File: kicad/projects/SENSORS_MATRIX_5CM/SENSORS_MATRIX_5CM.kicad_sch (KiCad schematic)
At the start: 15 parts, among them J1 Conn_02x11_Odd_Even

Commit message: sensors board almost finished
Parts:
- C1: LCSC p/n (none) -> C24123
- C2: MP CL21A105KOFNNNE -> (none); shop https://www.lcsc.com/product-detail/Multilayer-Ceramic-Capa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 -> (none)
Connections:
- net +3V3: now also J1.11 (Pin_11), J1.12 (Pin_12); no longer J1.2 (Pin_2), J1.20 (Pin_20)
- net FBK_3V3_SENSORS: now also J1.14 (Pin_14); no longer J1.19 (Pin_19)
- net GND: now also J1.20 (Pin_20)
- net SIG1: now also J1.2 (Pin_2); no longer J1.11 (Pin_11)
- net SIG2: now also J1.15 (Pin_15); no longer J1.14 (Pin_14)
- net SIG3: now also J1.18 (Pin_18); no longer J1.15 (Pin_15)
- net SIG4: now also J1.19 (Pin_19); no longer J1.18 (Pin_18)
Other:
- moved on the sheet: C1, C2, D1, D2, D3, D4, D5, J1, R26, R27, R3, R4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

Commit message: brain v2, all components placed?
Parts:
- J1: footprint Connector_PinSocket_2.54mm:PinSocket_2x11_P2.54mm_Horizontal -> Connector_PinHeader_2.54mm:PinHeader_2x11_P2.54mm_Horizontal
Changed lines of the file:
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@@
 	)
 	(junction
+		(at 161.29 63.5)
+		(diameter 0)
+		(color 0 0 0 0)
+	)
+	(junction
 		(at 217.17 54.61)
 		(diameter 0)
@@
 	)
 	(junction
+		(at 124.46 67.31)
+		(diameter 0)
+		(color 0 0 0 0)
+	)
+	(junction
 		(at 222.25 54.61)
 		(diameter 0)
@@
 	(wire
 		(pts
+			(xy 124.46 67.31) (xy 144.78 67.31)
+		)
+		(stroke
+			(width 0)
+			(type default)
+		)
+	)
+	(wire
+		(pts
 			(xy 157.48 69.85) (xy 165.1 69.85)
 		)
@@
 	(wire
 		(pts
-			(xy 121.92 67.31) (xy 144.78 67.31)
+			(xy 121.92 67.31) (xy 124.46 67.31)
 		)
 		(stroke
@@
 	(wire
 		(pts
+			(xy 161.29 63.5) (xy 132.08 63.5)
+		)
+		(stroke
+			(width 0)
+			(type default)
+		)
+	)
+	(wire
+		(pts
 			(xy 157.48 92.71) (xy 165.1 92.71)
 		)
@@
 	(wire
 		(pts
-			(xy 167.64 63.5) (xy 132.08 63.5)
+			(xy 167.64 63.5) (xy 161.29 63.5)
 		)
 		(stroke
@@
 	)
 	(symbol
+		(lib_id "power:PWR_FLAG")
+		(at 161.29 63.5 0)
+		(unit 1)
+		(exclude_from_sim no)
+		(in_bom yes)
+		(on_board yes)
+		(dnp no)
+		(fields_autoplaced yes)
+		(property "Reference" "#FLG01"
+			(at 161.29 61.595 0)
+			(effects
+				(font
+					(size 1.27 1.27)
+				)
+				(hide yes)
+			)
+		)
+		(property "Value" "PWR_FLAG"
+			(at 161.29 58.42 0)
+			(effects
+				(font
+					(size 1.27 1.27)
+				)
+			)
+		)
+		(property "Footprint" ""
+			(at 161.29 63.5 0)
+			(effects
+				(font
+					(size 1.27 1.27)
+				)
+				(hide yes)
+			)
+		)
+		(property "Datasheet" "~"
+			(at 161.29 63.5 0)
+			(effects
+				(font
+					(size 1.27 1.27)
+				)
+				(hide yes)
+			)
+		)
+		(property "Description" "Special symbol for telling ERC where power comes from"
+			(at 161.29 63.5 0)
+			(effects
+				(font
+					(size 1.27 1.27)
+				)
+				(hide yes)
+			)
+		)
+		(pin "1"
+		)
+		(instances
+			(project ""
+				(path "/9efc52ae-bc4a-45a9-ae90-3bdc8c654efe"
+					(reference "#FLG01")
+					(unit 1)
+				)
+			)
+		)
+	)
+	(symbol
 		(lib_id "power:+3V3")
 		(at 186.69 110.49 0)
@@
 			)
 		)
-		(property "Footprint" "Connector_PinSocket_2.54mm:PinSocket_2x11_P2.54mm_Horizontal"
+		(property "Footprint" "Connector_PinHeader_2.54mm:PinHeader_2x11_P2.54mm_Horizontal"
 			(at 149.86 80.01 0)
 			(effects
@@
 					(unit 1)
 				)
+			)
+		)
+	)
+	(symbol
+		(lib_id "power:PWR_FLAG")
+		(at 124.46 67.31 0)
+		(unit 1)
+		(exclude_from_sim no)
+		(in_bom yes)
+		(on_board yes)
+		(dnp no)
+		(fields_autoplaced yes)
+		(property "Reference" "#FLG02"
+			(at 124.46 65.405 0)
+			(effects
+				(font
+					(size 1.27 1.27)
+				)
+				(hide yes)
+			)
+		)
+		(property "Value" "PWR_FLAG"
+			(at 124.46 62.23 0)
+			(effects
+				(font
+					(size 1.27 1.27)
+				)
+			)
+		)
+		(property "Footprint" ""
+			(at 124.46 67.31 0)
+			(effects
+				(font
+					(size 1.27 1.27)
+				)
+				(hide yes)
+			)
+		)
+		(property "Datasheet" "~"
+			(at 124.46 67.31 0)
+			(effects
+				(font
+					(size 1.27 1.27)
+				)
+				(hide yes)
+			)
+		)
+		(property "Description" "Special symbol for telling ERC where power comes from"
+			(at 124.46 67.31 0)
+			(effects
+				(font
+					(size 1.27 1.27)
+				)
+				(hide yes)
+			)
+		)
+		(pin "1"
+		)
+		(instances
+			(project ""
+				(path "/9efc52ae-bc4a-45a9-ae90-3bdc8c654efe"
+					(reference "#FLG02")
+					(unit 1)
+				)

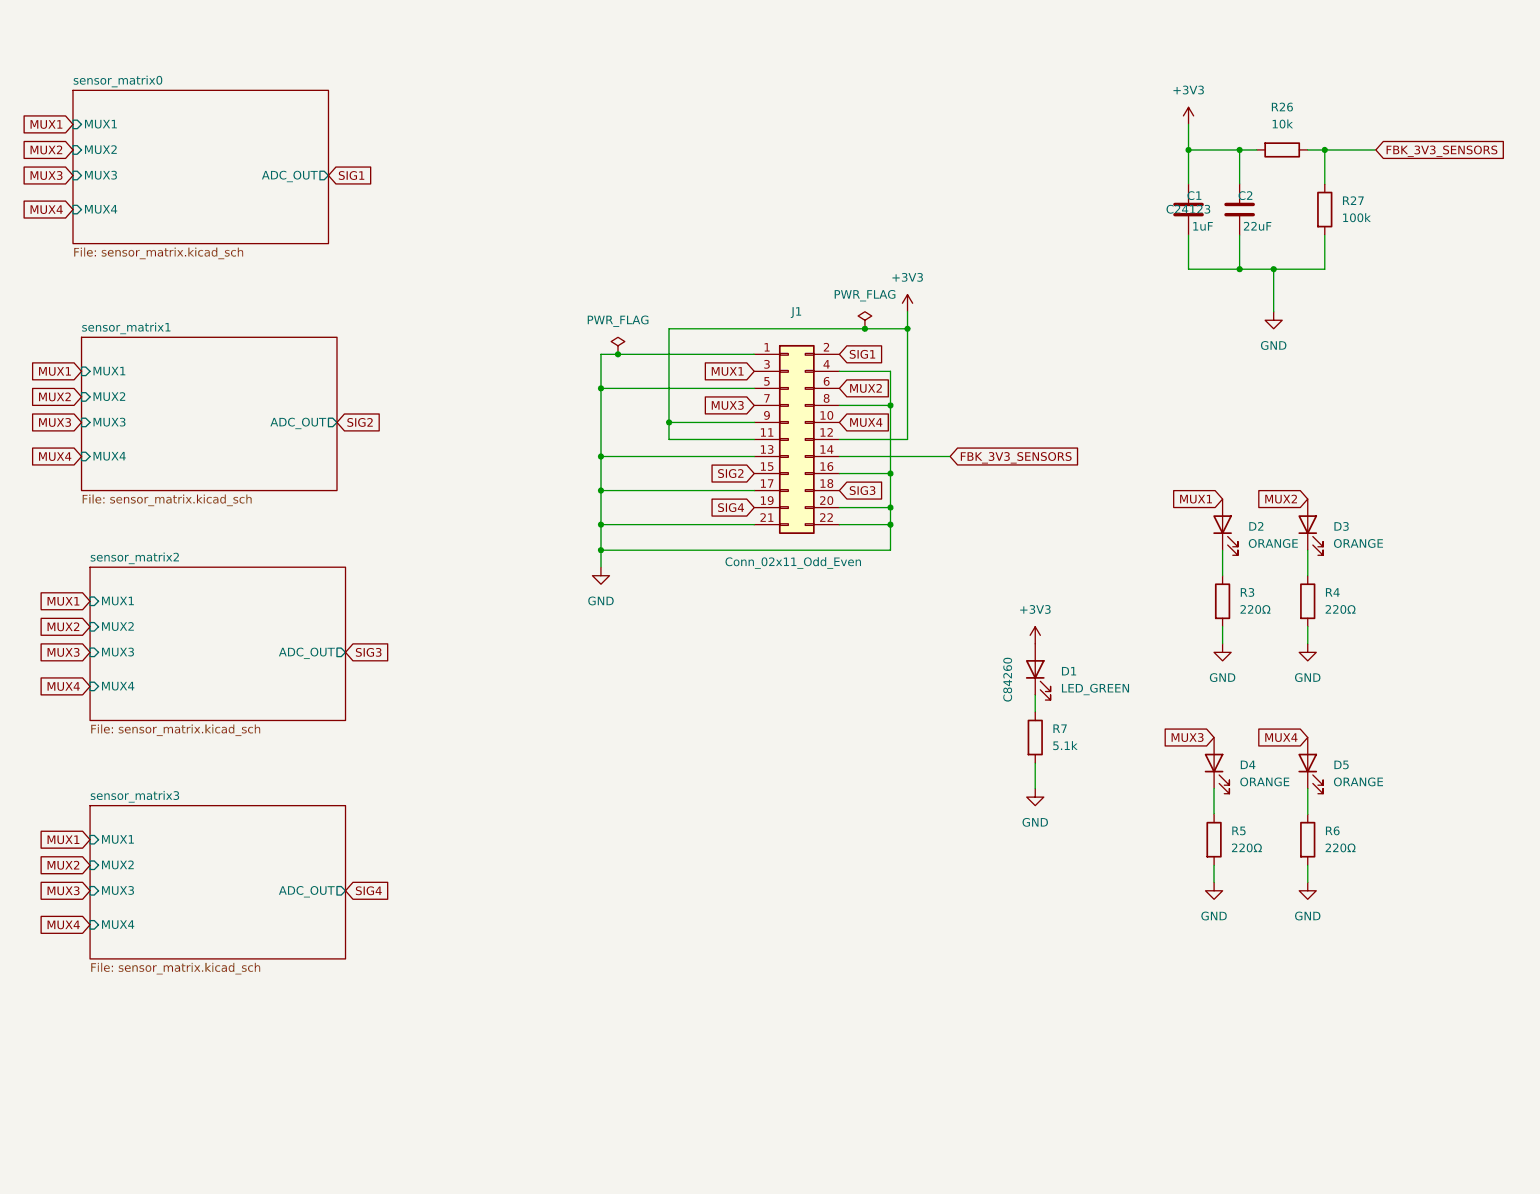
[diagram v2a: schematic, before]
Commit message: hw revisions and versions in schematic and pins
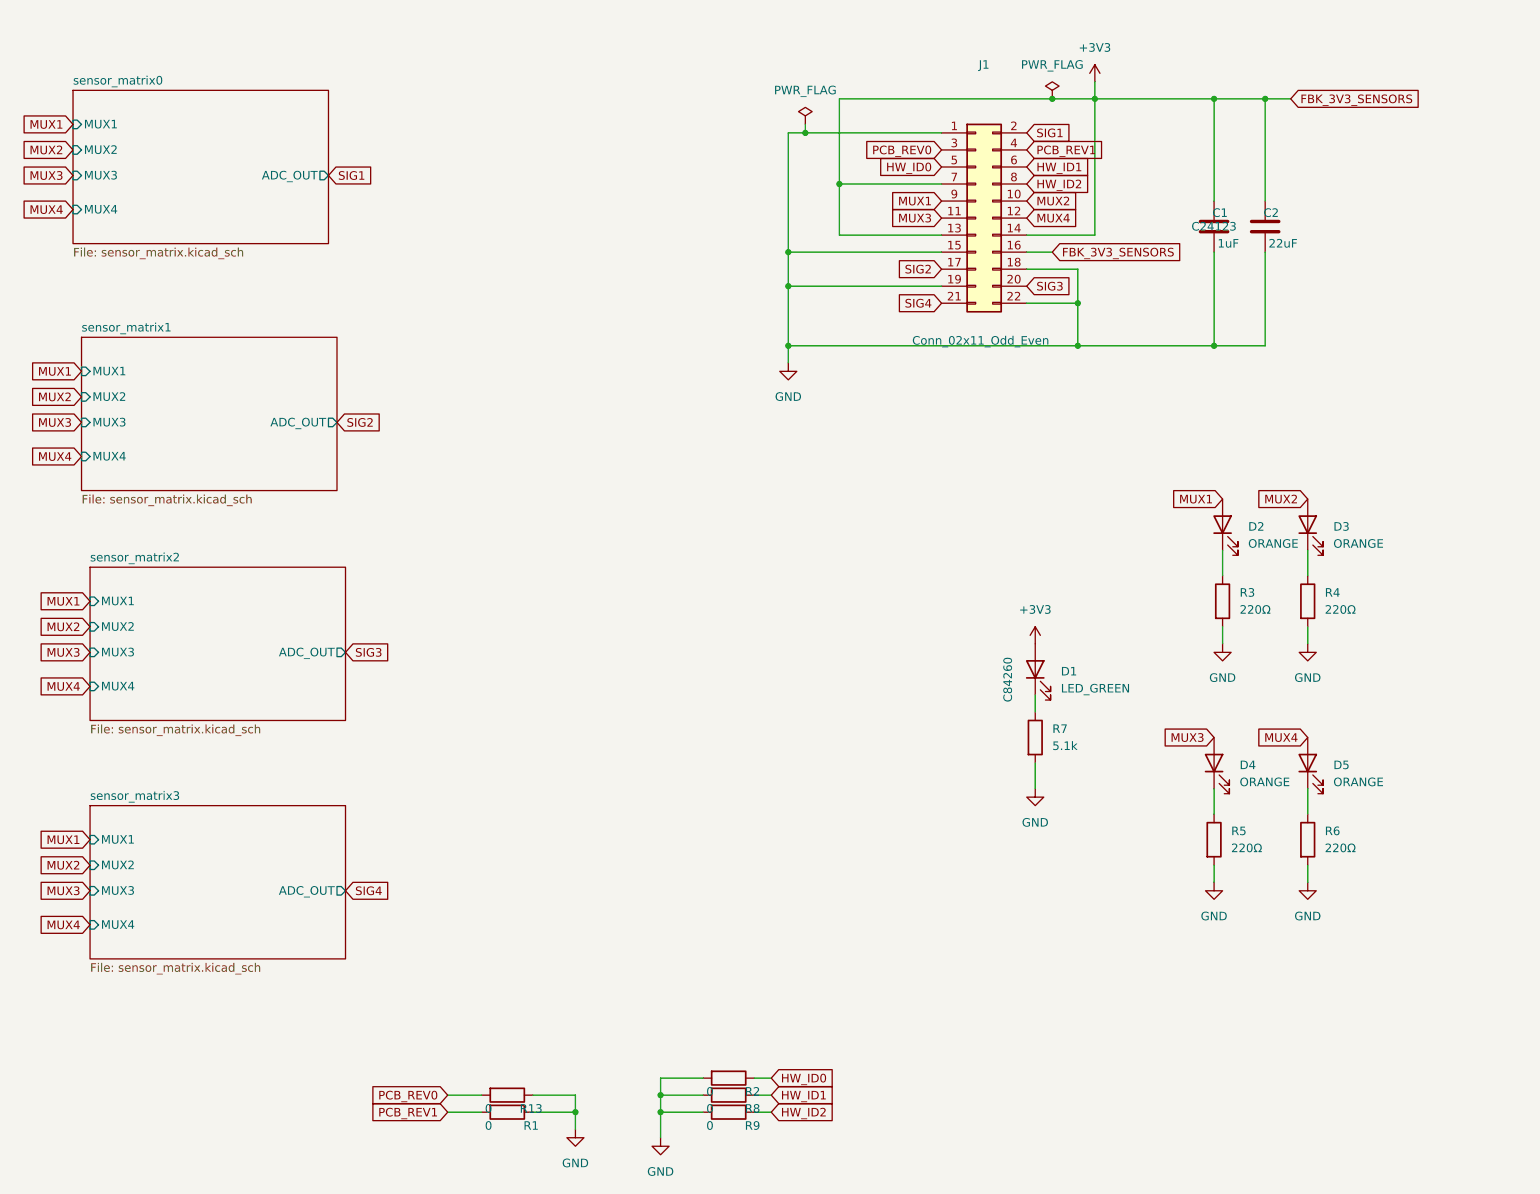
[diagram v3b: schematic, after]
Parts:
- removed R26: 10k, Resistor_SMD:R_0805_2012Metric_Pad1.20x1.40mm_HandSolder, symbol Device:R
- removed R27: 100k, Resistor_SMD:R_0805_2012Metric_Pad1.20x1.40mm_HandSolder, symbol Device:R
- added R1, R13, R2, R8, R9: 0, Resistor_SMD:R_0805_2012Metric_Pad1.20x1.40mm_HandSolder, symbol Device:R
- J1: footprint Connector_PinHeader_2.54mm:PinHeader_2x11_P2.54mm_Horizontal -> Connector_PinSocket_2.54mm:PinSocket_2x11_P2.54mm_Horizontal
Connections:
- net FBK_3V3_SENSORS is gone; now on net +3V3: J1.14 (Pin_14)
- net +3V3: now also J1.13 (Pin_13), J1.16 (Pin_16), J1.7 (Pin_7); no longer J1.11 (Pin_11), J1.12 (Pin_12), J1.9 (Pin_9)
- net GND: now also J1.15 (Pin_15), J1.18 (Pin_18), J1.19 (Pin_19), R1.1, R13.1, R2.2, R8.2, R9.2; no longer J1.13 (Pin_13), J1.16 (Pin_16), J1.17 (Pin_17), J1.20 (Pin_20), J1.21 (Pin_21), J1.4 (Pin_4), J1.5 (Pin_5), J1.8 (Pin_8)
- net MUX1: now also J1.9 (Pin_9); no longer J1.3 (Pin_3)
- net MUX2: now also J1.10 (Pin_10); no longer J1.6 (Pin_6)
- net MUX3: now also J1.11 (Pin_11); no longer J1.7 (Pin_7)
- net MUX4: now also J1.12 (Pin_12); no longer J1.10 (Pin_10)
- net SIG2: now also J1.17 (Pin_17); no longer J1.15 (Pin_15)
- net SIG3: now also J1.20 (Pin_20); no longer J1.18 (Pin_18)
- net SIG4: now also J1.21 (Pin_21); no longer J1.19 (Pin_19)
- new net HW_ID0: J1.5 (Pin_5), R2.1
- new net HW_ID1: J1.6 (Pin_6), R8.1
- new net HW_ID2: J1.8 (Pin_8), R9.1
- new net PCB_REV0: J1.3 (Pin_3), R13.2
- new net PCB_REV1: J1.4 (Pin_4), R1.2
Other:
- moved on the sheet: C1, C2, J1

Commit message: small adjustments
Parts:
- added R10: 0, Resistor_SMD:R_0805_2012Metric_Pad1.20x1.40mm_HandSolder, symbol Device:R
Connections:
- net +3V3: now also R10.2; no longer J1.16 (Pin_16)
- new net FBK_3V3_SENSORS: J1.16 (Pin_16), R10.1
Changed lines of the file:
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@@
+	(wire
+		(pts
+			(xy 232.41 29.21) (xy 236.22 29.21)
+		)
+		(stroke
+			(width 0)
+			(type default)
+		)
+	)
 	(wire
 		(pts
@@
 	(global_label "FBK_3V3_SENSORS"
 		(shape input)
-		(at 224.79 29.21 0)
-		(fields_autoplaced yes)
-		(effects
-			(font
-				(size 1.27 1.27)
-			)
-			(justify left)
-		)
-		(property "Intersheetrefs" "${INTERSHEET_REFS}"
-			(at 245.5551 29.21 0)
+		(at 236.22 29.21 0)
+		(fields_autoplaced yes)
+		(effects
+			(font
+				(size 1.27 1.27)
+			)
+			(justify left)
+		)
+		(property "Intersheetrefs" "${INTERSHEET_REFS}"
+			(at 256.9851 29.21 0)
 			(effects
 				(font
@@
 					(unit 1)
 				)
+			)
+		)
+	)
+	(symbol
+		(lib_id "Device:R")
+		(at 228.6 29.21 270)
+		(unit 1)
+		(exclude_from_sim no)
+		(in_bom yes)
+		(on_board yes)
+		(dnp no)
+		(property "Reference" "R10"
+			(at 232.156 31.242 90)
+			(effects
+				(font
+					(size 1.27 1.27)
+				)
+			)
+		)
+		(property "Value" "0"
+			(at 225.806 31.242 90)
+			(effects
+				(font
+					(size 1.27 1.27)
+				)
+			)
+		)
+		(property "Footprint" "Resistor_SMD:R_0805_2012Metric_Pad1.20x1.40mm_HandSolder"
+			(at 228.6 27.432 90)
+			(effects
+				(font
+					(size 1.27 1.27)
+				)
+				(hide yes)
+			)
+		)
+		(property "Datasheet" "~"
+			(at 228.6 29.21 0)
+			(effects
+				(font
+					(size 1.27 1.27)
+				)
+				(hide yes)
+			)
+		)
+		(property "Description" "Resistor"
+			(at 228.6 29.21 0)
+			(effects
+				(font
+					(size 1.27 1.27)
+				)
+				(hide yes)
+			)
+		)
+		(property "LCSC p/n" ""
+			(at 228.6 29.21 0)
+			(effects
+				(font
+					(size 1.27 1.27)
+				)
+			)
+		)
+		(pin "1"
+		)
+		(pin "2"
+		)
+		(instances
+			(project "SENSORS_MATRIX_5CM"
+				(path "/9efc52ae-bc4a-45a9-ae90-3bdc8c654efe"
+					(reference "R10")
+					(unit 1)
+				)

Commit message: sensors matrix with jlcpcb
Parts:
- C2: footprint Capacitor_SMD:C_0805_2012Metric_Pad1.18x1.45mm_HandSolder -> Capacitor_SMD:C_1206_3216Metric_Pad1.33x1.80mm_HandSolder; LCSC p/n (none) -> C5672; MP (none) -> CL31A226KPHNNNE; shop (none) -> https://www.lcsc.com/product-detail/C5672.html?s_z=n_q_c567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
- D2, D3, D4, D5: LCSC p/n (none) -> C434437; MP (none) -> SZYY0805O; shop (none) -> https://www.lcsc.com/product-detail/LED-Indication-Discrete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
- R1, R10, R13, R2, R8, R9: LCSC p/n (none) -> C96345; MP (none) -> RC0805JR-070RL; shop (none) -> https://www.lcsc.com/product-detail/C96345.html?s_z=n_q_t_r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
- R3, R4, R5, R6: LCSC p/n (none) -> C114519; MP (none) -> RC0805FR-07220RL; shop (none) -> https://www.lcsc.com/product-detail/C114519.html?s_z=n_q_t_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
